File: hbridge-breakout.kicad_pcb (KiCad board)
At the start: 2 copper layers, 28.5 x 38.6 mm, 14 parts, among them J1 Conn_01x10, J2 Conn_01x04, J3 Conn_01x08, U1 74HC00, U2 DRV8870DDA

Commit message: Added JLCJLCJLCJLC
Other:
- board text added: "JLCJLCJLCJLC"
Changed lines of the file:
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@@
     (effects (font (size 1.5 1.5) (thickness 0.3) bold) (justify left bottom mirror))
+  )
+  (gr_text "JLCJLCJLCJLC" (at 159.6 85.7) (layer "F.SilkS")
+    (effects (font (size 1 1) (thickness 0.15)) (justify left bottom))
   )
   (segment (start 154.6625 86.6) (end 164.720822 86.6) (width 1) (layer "F.Cu") (net 1))

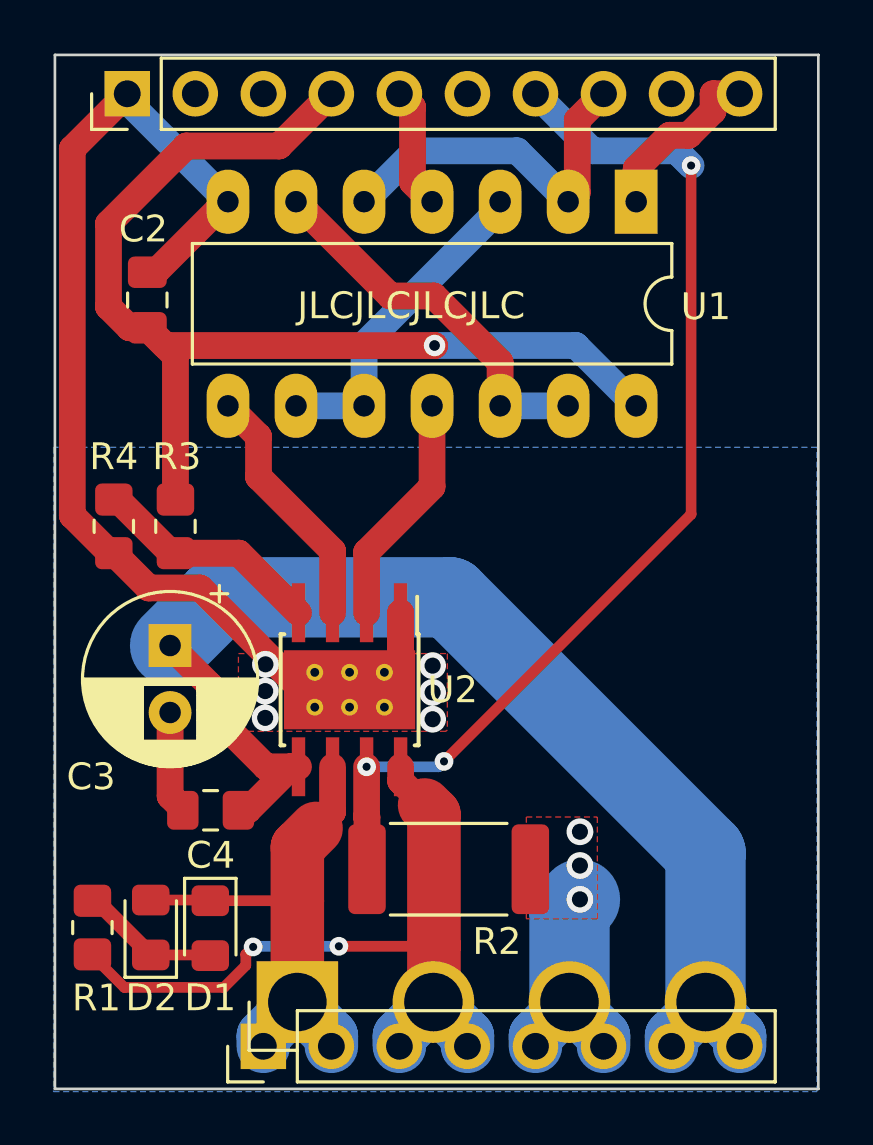
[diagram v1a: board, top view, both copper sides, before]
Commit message: Moved current sense via away from chip pin pad, thickened trace.
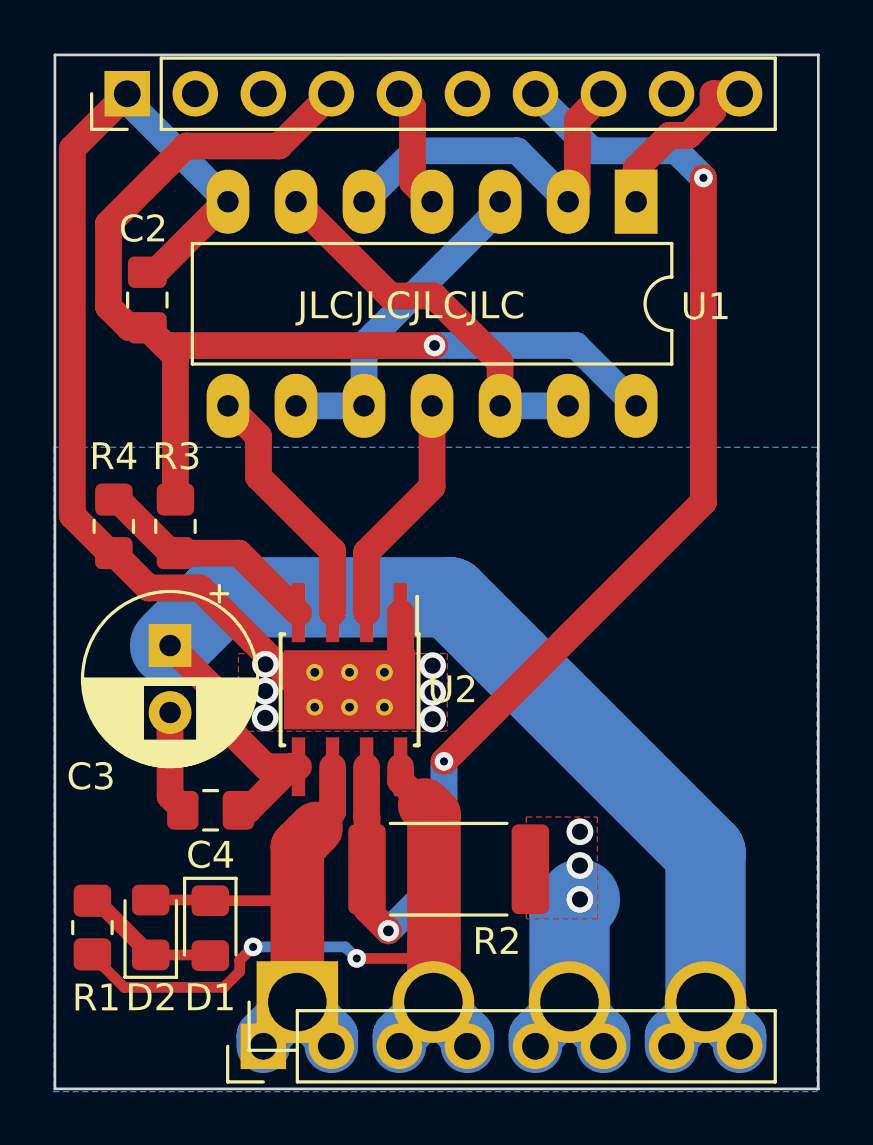
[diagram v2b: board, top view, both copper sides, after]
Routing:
- net /CS: track 39.8 -> 47.0 mm
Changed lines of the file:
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@@
   (segment (start 163.41 77.2) (end 163.9 77.69) (width 1) (layer "F.Cu") (net 7))
   (segment (start 163.9 80.5) (end 164.63 81.23) (width 1) (layer "F.Cu") (net 7))
+  (segment (start 174.76 80.34) (end 174.76 92.44) (width 1) (layer "F.Cu") (net 9))
   (segment (start 162.2 106.15) (end 162.2 104.2) (width 1) (layer "F.Cu") (net 9))
   (segment (start 162.185 102.325) (end 162.185 104.185) (width 1) (layer "F.Cu") (net 9))
   (segment (start 162.2 104.2) (end 162.185 104.185) (width 1) (layer "F.Cu") (net 9))
-  (segment (start 174.3 92.9) (end 174.3 79.88) (width 0.4) (layer "F.Cu") (net 9))
-  (segment (start 165.075 102.125) (end 174.3 92.9) (width 0.4) (layer "F.Cu") (net 9))
-  (via (at 174.3 79.88) (size 0.7) (drill 0.3) (layers "F.Cu" "B.Cu") (net 9))
+  (segment (start 162.2 107.65) (end 163 108.45) (width 1) (layer "F.Cu") (net 9))
+  (segment (start 174.76 92.44) (end 165.075 102.125) (width 1) (layer "F.Cu") (net 9))
+  (segment (start 162.2 106.15) (end 162.2 107.65) (width 1) (layer "F.Cu") (net 9))
+  (via (at 174.76 80.34) (size 0.7) (drill 0.3) (layers "F.Cu" "B.Cu") (net 9))
+  (via (at 163 108.45) (size 0.8) (drill 0.4) (layers "F.Cu" "B.Cu") (net 9))
   (via (at 165.075 102.125) (size 0.7) (drill 0.3) (layers "F.Cu" "B.Cu") (net 9))
-  (via (at 162.185 102.325) (size 0.7) (drill 0.3) (layers "F.Cu" "B.Cu") (net 9))
-  (segment (start 164.875 102.325) (end 165.075 102.125) (width 0.4) (layer "B.Cu") (net 9))
-  (segment (start 173.75 79.33) (end 174.3 79.88) (width 1) (layer "B.Cu") (net 9))
+  (segment (start 165.075 102.125) (end 165.075 106.375) (width 1) (layer "B.Cu") (net 9))
+  (segment (start 168.49 77.2) (end 170.62 79.33) (width 1) (layer "B.Cu") (net 9))
+  (segment (start 173.75 79.33) (end 174.76 80.34) (width 1) (layer "B.Cu") (net 9))
   (segment (start 170.62 79.33) (end 173.75 79.33) (width 1) (layer "B.Cu") (net 9))
-  (segment (start 168.49 77.2) (end 170.62 79.33) (width 1) (layer "B.Cu") (net 9))
-  (segment (start 162.185 102.325) (end 164.875 102.325) (width 0.4) (layer "B.Cu") (net 9))
+  (segment (start 165.075 106.375) (end 163 108.45) (width 1) (layer "B.Cu") (net 9))
   (segment (start 169.71 81.23) (end 170.05 80.89) (width 1) (layer "F.Cu") (net 10))
   (segment (start 170.05 80.89) (end 170.05 78.18) (width 1) (layer "F.Cu") (net 10))
@@
   (segment (start 174.212032 78.75) (end 173.5 78.75) (width 1) (layer "F.Cu") (net 12))
   (segment (start 163.455 102.325) (end 163.455 102.855) (width 1) (layer "F.Cu") (net 13))
+  (segment (start 157.45 109.969239) (end 157.45 109.55) (width 0.4) (layer "F.Cu") (net 13))
   (segment (start 153.13875 110.56125) (end 156.857989 110.56125) (width 0.4) (layer "F.Cu") (net 13))
-  (segment (start 156.857989 110.56125) (end 157.676 109.743239) (width 0.4) (layer "F.Cu") (net 13))
+  (segment (start 164.7 109) (end 164.2195 109.4805) (width 0.4) (layer "F.Cu") (net 13))
+  (segment (start 156.857989 110.56125) (end 157.45 109.969239) (width 0.4) (layer "F.Cu") (net 13))
   (segment (start 164.68 111.109) (end 164.7 111.089) (width 2) (layer "F.Cu") (net 13))
-  (segment (start 164.673791 109.026209) (end 164.7 109) (width 0.4) (layer "F.Cu") (net 13))
-  (segment (start 153.13875 110.56125) (end 151.95 109.3725) (width 0.4) (layer "F.Cu") (net 13))
-  (segment (start 157.676 109.743239) (end 157.676 109.324) (width 0.4) (layer "F.Cu") (net 13))
+  (segment (start 157.45 109.55) (end 157.95 109.05) (width 0.4) (layer "F.Cu") (net 13))
   (segment (start 163.455 102.855) (end 164.35 103.75) (width 1) (layer "F.Cu") (net 13))
-  (segment (start 161.15 109.026209) (end 164.673791 109.026209) (width 0.4) (layer "F.Cu") (net 13))
+  (segment (start 164.2195 109.4805) (end 161.8195 109.4805) (width 0.4) (layer "F.Cu") (net 13))
+  (segment (start 151.95 109.3725) (end 153.13875 110.56125) (width 0.4) (layer "F.Cu") (net 13))
   (segment (start 164.7 104.1) (end 164.35 103.75) (width 2) (layer "F.Cu") (net 13))
   (segment (start 164.7 109) (end 164.7 104.1) (width 2) (layer "F.Cu") (net 13))
-  (segment (start 157.676 109.324) (end 157.95 109.05) (width 0.4) (layer "F.Cu") (net 13))
   (segment (start 164.7 111.089) (end 164.7 109) (width 2) (layer "F.Cu") (net 13))
   (via (at 157.95 109.05) (size 0.7) (drill 0.3) (layers "F.Cu" "B.Cu") (net 13))
-  (via (at 161.15 109.026209) (size 0.7) (drill 0.3) (layers "F.Cu" "B.Cu") (net 13))
+  (via (at 161.8195 109.4805) (size 0.7) (drill 0.3) (layers "F.Cu" "B.Cu") (net 13))
   (segment (start 165.95 112.76) (end 165.95 112.379) (width 2) (layer "B.Cu") (net 13))
-  (segment (start 157.973791 109.026209) (end 161.15 109.026209) (width 0.4) (layer "B.Cu") (net 13))
+  (segment (start 161.389 109.05) (end 161.8195 109.4805) (width 0.4) (layer "B.Cu") (net 13))
   (segment (start 165.95 112.379) (end 164.68 111.109) (width 2) (layer "B.Cu") (net 13))
   (segment (start 163.41 112.379) (end 164.68 111.109) (width 2) (layer "B.Cu") (net 13))
+  (segment (start 157.95 109.05) (end 161.389 109.05) (width 0.4) (layer "B.Cu") (net 13))
   (segment (start 163.41 112.76) (end 163.41 112.379) (width 2) (layer "B.Cu") (net 13))
-  (segment (start 157.95 109.05) (end 157.973791 109.026209) (width 0.4) (layer "B.Cu") (net 13))
   (segment (start 157.42 94.35) (end 159.645 96.575) (width 1) (layer "F.Cu") (net 14))
   (segment (start 152.75 92.35) (end 152.893503 92.35) (width 1) (layer "F.Cu") (net 14))
